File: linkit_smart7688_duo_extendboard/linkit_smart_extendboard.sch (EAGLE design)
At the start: 25 parts, among them U1 BME280

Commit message: revision PCB layout
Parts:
- added U$4: PIN2MM, pin_2mm:PIN2MM
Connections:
- net +5V: now also U$4.5V
- net GND: now also U$4.GND
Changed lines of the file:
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@@
 </class>
 </classes>
+<modules>
+<module name="PIN" prefix="" dx="30.48" dy="20.32">
+<ports>
+</ports>
+<variantdefs>
+</variantdefs>
+<parts>
+</parts>
+<sheets>
+<sheet>
+<plain>
+</plain>
+<instances>
+</instances>
+<busses>
+</busses>
+<nets>
+</nets>
+</sheet>
+</sheets>
+</module>
+</modules>
 <parts>
 <part name="U$1" library="linkit7688" deviceset="LINKIT7688" device=""/>
@@
 <part name="+3V6" library="supply1" deviceset="+3V3" device=""/>
 <part name="+3V7" library="supply1" deviceset="+3V3" device=""/>
+<part name="U$4" library="pin_2mm" deviceset="PIN2MM" device=""/>
+<part name="P+6" library="supply1" deviceset="+5V" device=""/>
+<part name="GND23" library="supply1" deviceset="GND" device=""/>
 </parts>
 <sheets>
@@
 <instance part="+3V6" gate="G$1" x="76.2" y="27.94" rot="R90"/>
 <instance part="+3V7" gate="G$1" x="76.2" y="12.7" rot="R90"/>
+<instance part="U$4" gate="G$1" x="-66.04" y="-15.24"/>
+<instance part="P+6" gate="1" x="-73.66" y="10.16" rot="R90"/>
+<instance part="GND23" gate="1" x="-71.12" y="-12.7"/>
 </instances>
 <busses>
@@
 <junction x="83.82" y="-7.62"/>
 </segment>
+<segment>
+<pinref part="U$4" gate="G$1" pin="5V"/>
+<pinref part="P+6" gate="1" pin="+5V"/>
+<junction x="-71.12" y="10.16"/>
+</segment>
 </net>
 <net name="+3V3" class="0">
@@
 <junction x="167.64" y="93.98"/>
 </segment>
+<segment>
+<pinref part="U$4" gate="G$1" pin="GND"/>
+<pinref part="GND23" gate="1" pin="GND"/>
+<junction x="-71.12" y="-10.16"/>
+</segment>
 </net>

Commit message: update PCB layout for RP1135C box
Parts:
- renumbered Q1 to BSS138N_01, Q2 to BSS138N_02
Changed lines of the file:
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@@
 <part name="U1" library="BME280ComponentLibrary" deviceset="BME280" device="" value="BME280"/>
 <part name="GND22" library="supply1" deviceset="GND" device=""/>
-<part name="Q1" library="adafruit" deviceset="MOSFET-N" device="WAVE"/>
-<part name="Q2" library="adafruit" deviceset="MOSFET-N" device="WAVE"/>
+<part name="BSS138N_01" library="adafruit" deviceset="MOSFET-N" device="WAVE"/>
+<part name="BSS138N_02" library="adafruit" deviceset="MOSFET-N" device="WAVE"/>
 <part name="+3V6" library="supply1" deviceset="+3V3" device=""/>
 <part name="+3V7" library="supply1" deviceset="+3V3" device=""/>
@@
 <instance part="U1" gate="U1" x="182.88" y="101.6"/>
 <instance part="GND22" gate="1" x="167.64" y="91.44"/>
-<instance part="Q1" gate="G$1" x="86.36" y="30.48"/>
-<instance part="Q2" gate="G$1" x="86.36" y="15.24"/>
+<instance part="BSS138N_01" gate="G$1" x="86.36" y="30.48"/>
+<instance part="BSS138N_02" gate="G$1" x="86.36" y="15.24"/>
 <instance part="+3V6" gate="G$1" x="76.2" y="27.94" rot="R90"/>
 <instance part="+3V7" gate="G$1" x="76.2" y="12.7" rot="R90"/>
@@
 </segment>
 <segment>
-<pinref part="Q1" gate="G$1" pin="G"/>
+<pinref part="BSS138N_01" gate="G$1" pin="G"/>
 <pinref part="+3V6" gate="G$1" pin="+3V3"/>
 <wire x1="78.74" y1="27.94" x2="83.82" y2="27.94" width="0.1524" layer="91"/>
@@
 </segment>
 <segment>
-<pinref part="Q2" gate="G$1" pin="G"/>
+<pinref part="BSS138N_02" gate="G$1" pin="G"/>
 <pinref part="+3V7" gate="G$1" pin="+3V3"/>
 <wire x1="78.74" y1="12.7" x2="83.82" y2="12.7" width="0.1524" layer="91"/>
@@
 </segment>
 <segment>
-<pinref part="Q2" gate="G$1" pin="S"/>
+<pinref part="BSS138N_02" gate="G$1" pin="S"/>
 <wire x1="114.3" y1="10.16" x2="88.9" y2="10.16" width="0.1524" layer="91"/>
 <junction x="88.9" y="10.16"/>
@@
 </segment>
 <segment>
-<pinref part="Q1" gate="G$1" pin="S"/>
+<pinref part="BSS138N_01" gate="G$1" pin="S"/>
 <wire x1="88.9" y1="25.4" x2="111.76" y2="25.4" width="0.1524" layer="91"/>
 <junction x="88.9" y="25.4"/>
@@
 <segment>
 <wire x1="142.24" y1="25.4" x2="124.46" y2="25.4" width="0.1524" layer="91"/>
-<pinref part="Q1" gate="G$1" pin="D"/>
+<pinref part="BSS138N_01" gate="G$1" pin="D"/>
 <wire x1="124.46" y1="25.4" x2="124.46" y2="35.56" width="0.1524" layer="91"/>
 <wire x1="124.46" y1="35.56" x2="88.9" y2="35.56" width="0.1524" layer="91"/>
@@
 <segment>
 <wire x1="142.24" y1="22.86" x2="96.52" y2="22.86" width="0.1524" layer="91"/>
-<pinref part="Q2" gate="G$1" pin="D"/>
+<pinref part="BSS138N_02" gate="G$1" pin="D"/>
 <wire x1="96.52" y1="22.86" x2="96.52" y2="20.32" width="0.1524" layer="91"/>
 <wire x1="96.52" y1="20.32" x2="88.9" y2="20.32" width="0.1524" layer="91"/>

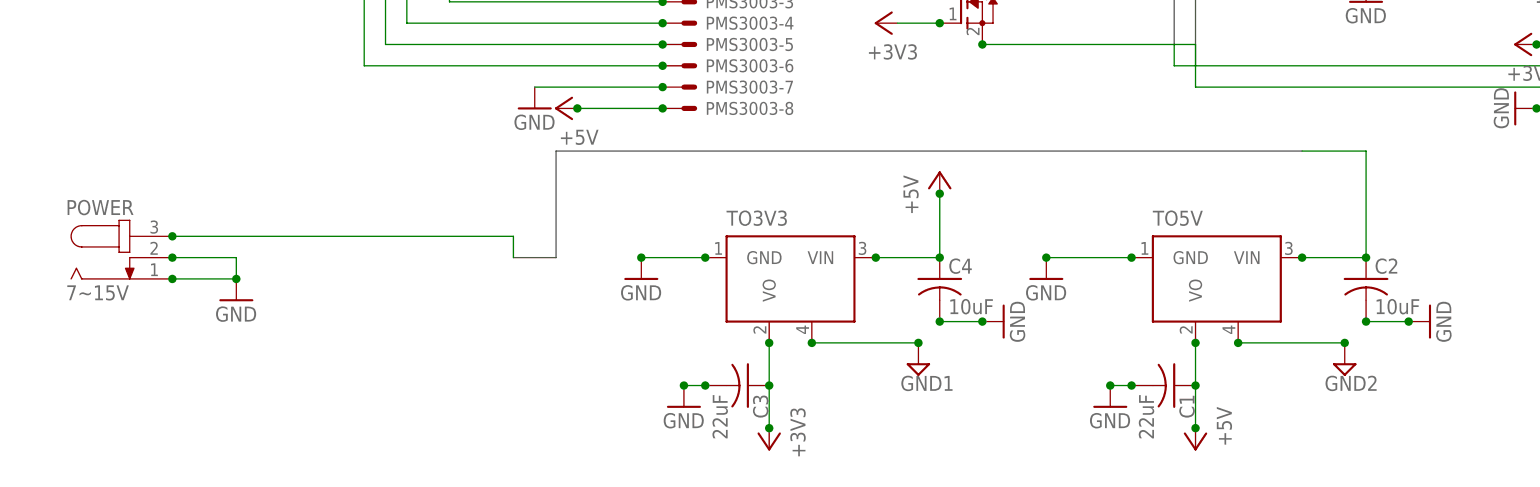
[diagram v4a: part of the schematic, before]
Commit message: add dimension in 3dm, remove 5v LDO on .brd & sch .file we don't need them any more, because the DC in is already 5v
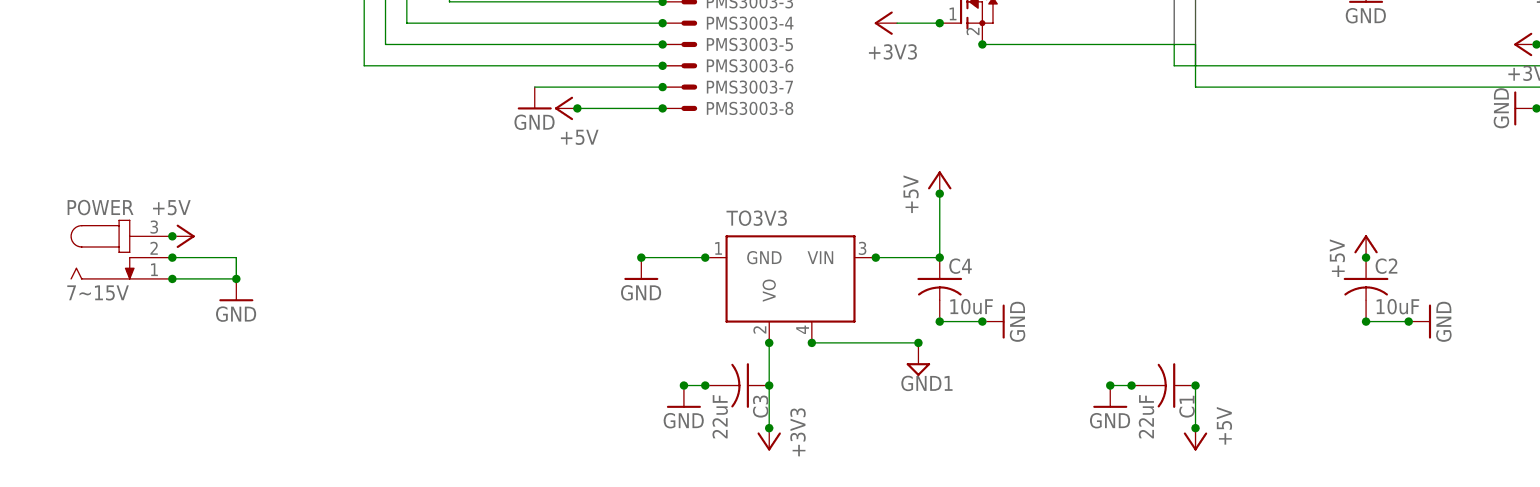
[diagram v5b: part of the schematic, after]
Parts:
- removed TO5V: LM2936MP-3.0, national-semiconductor:LM2936MP-3.0
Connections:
- removed net B$1: C2.1, POWER.3, TO5V.VIN
- removed net GND2: TO5V.HS
- net +5V: now also C2.1, POWER.3; no longer TO5V.VO
- net GND: no longer TO5V.GND
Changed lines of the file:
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@@
 <part name="TO3V3" library="national-semiconductor" deviceset="LM2936MP?*" device="" technology="-3.0"/>
 <part name="POWER" library="con-jack" deviceset="JACK-PLUG" device="0" value="7~15V"/>
-<part name="TO5V" library="national-semiconductor" deviceset="LM2936MP?*" device="" technology="-3.0"/>
 <part name="3V3D" library="Connector_grove" deviceset="TWIG-4P-2.0" device="-2.0"/>
 <part name="3V3I2C" library="Connector_grove_i2c" deviceset="TWIG-4P-2.0" device="-2.0"/>
@@
 <part name="GND4" library="supply1" deviceset="GND" device=""/>
 <part name="GND5" library="supply1" deviceset="GND" device=""/>
-<part name="GND6" library="supply1" deviceset="GND" device=""/>
 <part name="GND8" library="supply1" deviceset="GND" device=""/>
 <part name="GND9" library="supply1" deviceset="GND" device=""/>
@@
 <part name="GND7" library="supply1" deviceset="GND" device=""/>
 <part name="SUPPLY1" library="supply2" deviceset="GND1" device=""/>
-<part name="SUPPLY2" library="supply2" deviceset="GND2" device=""/>
 <part name="GND12" library="supply1" deviceset="GND" device=""/>
 <part name="GND13" library="supply1" deviceset="GND" device=""/>
@@
 <part name="P+6" library="supply1" deviceset="+5V" device=""/>
 <part name="GND23" library="supply1" deviceset="GND" device=""/>
+<part name="P+8" library="supply1" deviceset="+5V" device=""/>
+<part name="P+9" library="supply1" deviceset="+5V" device=""/>
 </parts>
 <sheets>
@@
 </instance>
 <instance part="POWER" gate="G$1" x="-12.7" y="-15.24"/>
-<instance part="TO5V" gate="G$1" x="116.84" y="-17.78" smashed="yes">
-<attribute name="NAME" x="109.22" y="-11.43" size="1.778" layer="95"/>
-</instance>
 <instance part="3V3D" gate="G$1" x="144.78" y="74.93" smashed="yes">
 <attribute name="NAME" x="139.7" y="80.772" size="1.27" layer="95"/>
@@
 <instance part="GND4" gate="1" x="134.62" y="15.24"/>
 <instance part="GND5" gate="1" x="48.26" y="-17.78"/>
-<instance part="GND6" gate="1" x="96.52" y="-17.78"/>
 <instance part="GND8" gate="1" x="0" y="-20.32"/>
 <instance part="GND9" gate="1" x="-55.88" y="53.34" rot="R90"/>
@@
 <instance part="GND7" gate="1" x="35.56" y="2.54"/>
 <instance part="SUPPLY1" gate="G$1" x="81.28" y="-27.94"/>
-<instance part="SUPPLY2" gate="G$1" x="132.08" y="-27.94"/>
 <instance part="GND12" gate="1" x="104.14" y="-33.02"/>
 <instance part="GND13" gate="1" x="142.24" y="-22.86" rot="R90"/>
@@
 <instance part="P+6" gate="1" x="-73.66" y="10.16" rot="R90"/>
 <instance part="GND23" gate="1" x="-71.12" y="-12.7"/>
+<instance part="P+8" gate="1" x="-5.08" y="-12.7" rot="R270"/>
+<instance part="P+9" gate="1" x="134.62" y="-12.7"/>
 </instances>
 <busses>
@@
 <wire x1="111.76" y1="60.96" x2="111.76" y2="10.16" width="0.762" layer="92"/>
 <label x="104.14" y="55.88" size="1.778" layer="95"/>
-</segment>
-</bus>
-<bus name="B$1">
-<segment>
-<wire x1="33.02" y1="-15.24" x2="38.1" y2="-15.24" width="0.762" layer="92"/>
-<wire x1="38.1" y1="-15.24" x2="38.1" y2="-2.54" width="0.762" layer="92"/>
-<wire x1="38.1" y1="-2.54" x2="127" y2="-2.54" width="0.762" layer="92"/>
 </segment>
 </bus>
@@
 </segment>
 <segment>
-<pinref part="TO5V" gate="G$1" pin="VO"/>
 <pinref part="P+1" gate="1" pin="+5V"/>
-<wire x1="114.3" y1="-25.4" x2="114.3" y2="-30.48" width="0.1524" layer="91"/>
 <pinref part="C1" gate="G$1" pin="1"/>
 <wire x1="114.3" y1="-30.48" x2="114.3" y2="-35.56" width="0.1524" layer="91"/>
+<junction x="114.3" y="-35.56"/>
 <junction x="114.3" y="-30.48"/>
-<junction x="114.3" y="-25.4"/>
-<junction x="114.3" y="-35.56"/>
 </segment>
 <segment>
@@
 <junction x="-71.12" y="10.16"/>
 </segment>
+<segment>
+<pinref part="POWER" gate="G$1" pin="3"/>
+<pinref part="P+8" gate="1" pin="+5V"/>
+<junction x="-7.62" y="-12.7"/>
+</segment>
+<segment>
+<pinref part="C2" gate="G$1" pin="1"/>
+<pinref part="P+9" gate="1" pin="+5V"/>
+<junction x="134.62" y="-15.24"/>
+</segment>
 </net>
 <net name="+3V3" class="0">
@@
 <junction x="55.88" y="-15.24"/>
 <junction x="48.26" y="-15.24"/>
-</segment>
-<segment>
-<pinref part="TO5V" gate="G$1" pin="GND"/>
-<pinref part="GND6" gate="1" pin="GND"/>
-<wire x1="96.52" y1="-15.24" x2="106.68" y2="-15.24" width="0.1524" layer="91"/>
-<junction x="96.52" y="-15.24"/>
-<junction x="106.68" y="-15.24"/>
 </segment>
 <segment>
@@
 <wire x1="111.76" y1="7.62" x2="167.64" y2="7.62" width="0.1524" layer="91"/>
 <junction x="167.64" y="7.62"/>
-</segment>
-</net>
-<net name="B$1" class="0">
-<segment>
-<wire x1="127" y1="-2.54" x2="134.62" y2="-2.54" width="0.1524" layer="91"/>
-<wire x1="134.62" y1="-2.54" x2="134.62" y2="-15.24" width="0.1524" layer="91"/>
-<pinref part="TO5V" gate="G$1" pin="VIN"/>
-<wire x1="134.62" y1="-15.24" x2="127" y2="-15.24" width="0.1524" layer="91"/>
-<pinref part="C2" gate="G$1" pin="1"/>
-<junction x="134.62" y="-15.24"/>
-<junction x="127" y="-15.24"/>
-</segment>
-<segment>
-<pinref part="POWER" gate="G$1" pin="3"/>
-<wire x1="33.02" y1="-15.24" x2="33.02" y2="-12.7" width="0.1524" layer="91"/>
-<wire x1="33.02" y1="-12.7" x2="-7.62" y2="-12.7" width="0.1524" layer="91"/>
-<junction x="-7.62" y="-12.7"/>
 </segment>
 </net>
@@
 </segment>
 </net>
-<net name="GND2" class="0">
-<segment>
-<pinref part="SUPPLY2" gate="G$1" pin="GND2"/>
-<pinref part="TO5V" gate="G$1" pin="HS"/>
-<wire x1="132.08" y1="-25.4" x2="119.38" y2="-25.4" width="0.1524" layer="91"/>
-<junction x="132.08" y="-25.4"/>
-<junction x="119.38" y="-25.4"/>
-</segment>
-</net>
